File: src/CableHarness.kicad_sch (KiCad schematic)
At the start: 15 parts, among them J64 MiniFit_2x02_M, J66 Banana F, J67 Banana F, J68 Banana F, J69 Banana F, J70 Banana F, J71 Banana F, J74 MiniFit_2x02_M, J75 MiniFit_2x02_M, J76 Barrel_Jack F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

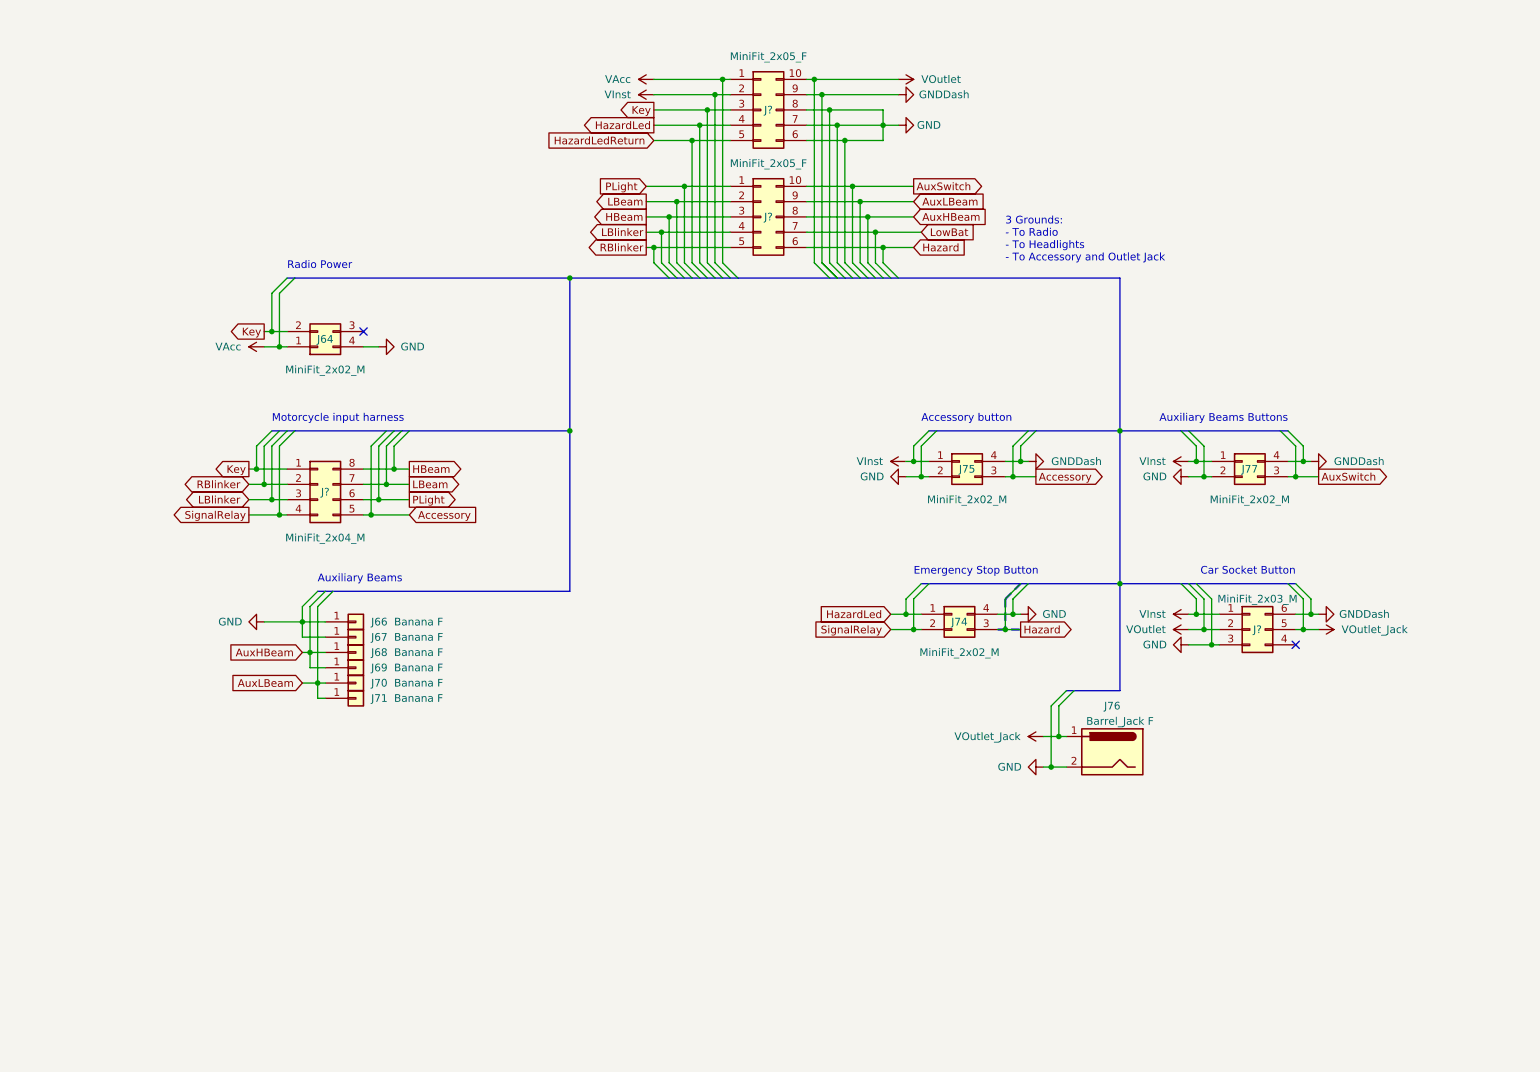
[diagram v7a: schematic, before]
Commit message: Fix battery sensor
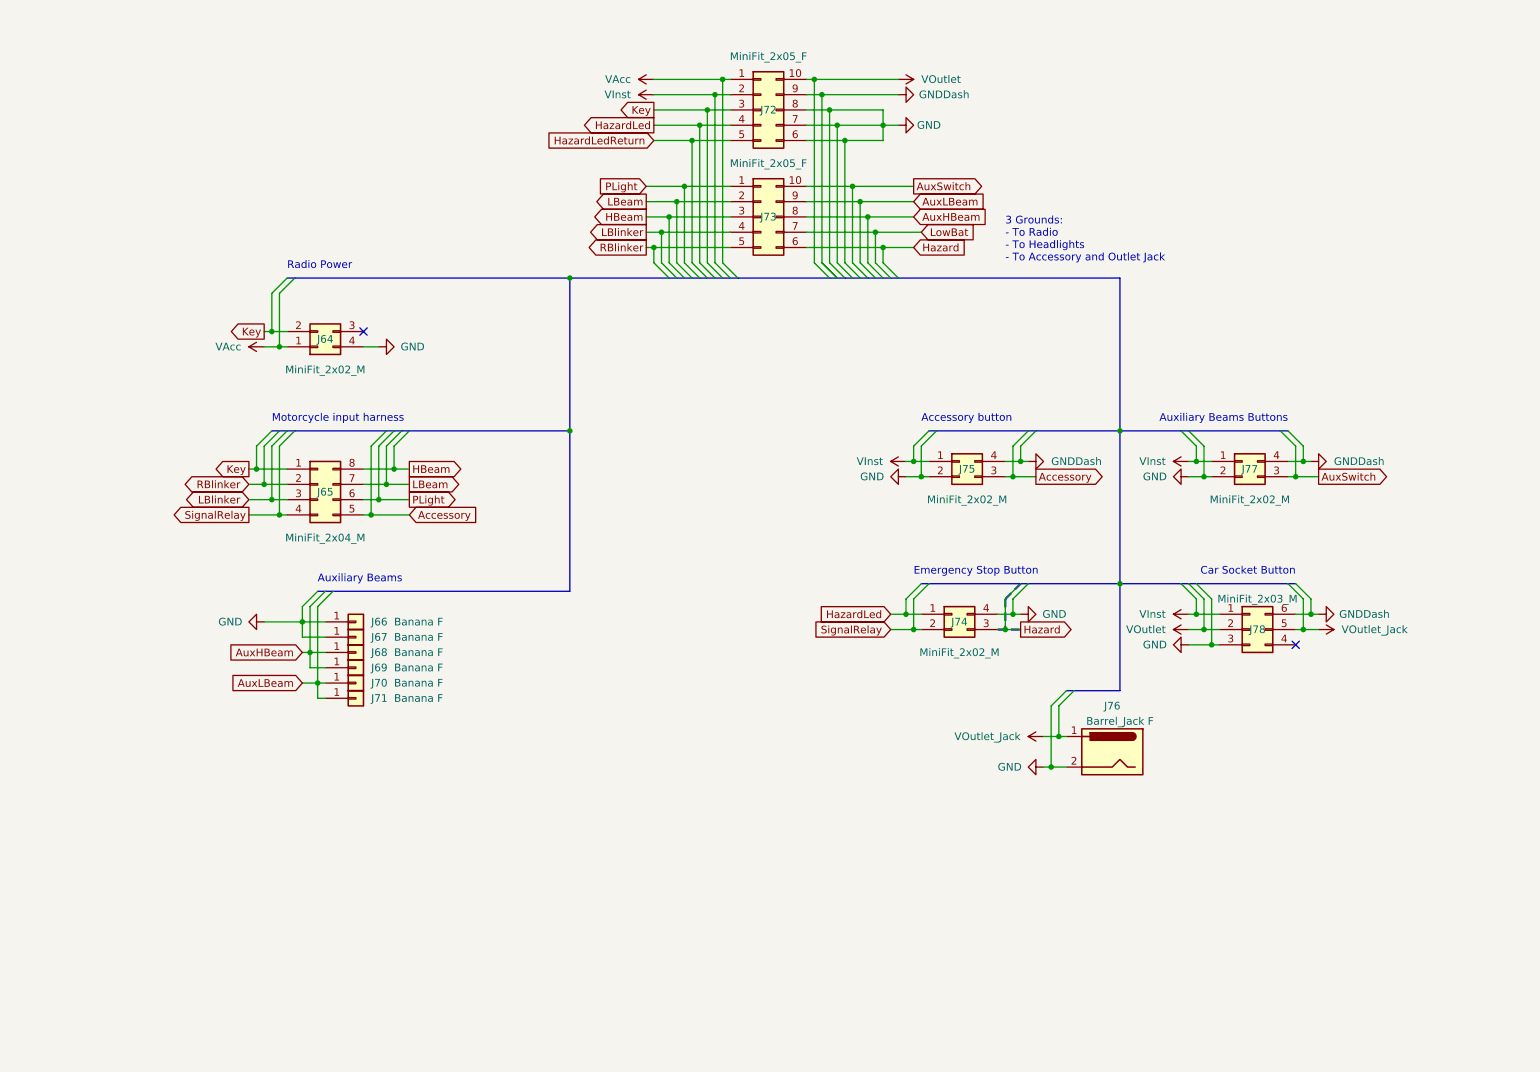
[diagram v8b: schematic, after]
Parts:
- gave numbers to parts that had none: 4
